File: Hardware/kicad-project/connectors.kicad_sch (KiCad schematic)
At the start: 25 parts, among them CN10 Conn_02x17_Odd_Even, CN7 Conn_02x10_Odd_Even, CN8 Conn_02x08_Odd_Even, CN9 Conn_02x15_Odd_Even, J1 Brake connector, J2 Conn_01x08, J3 PWM module connector, J5 UART Connector, J6 Stepper supply, Q1 Q_NMOS_DGS

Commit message: hw: update layout corrections
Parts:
- Q1: symbol Device:Q_NMOS_DGS -> Device:Q_NMOS_GDS
- TP1: renamed from TP_24V; value TestPoint -> 24V
- TP2: renamed from TP_TORQUE; value TestPoint -> TORQUE
- TP3: renamed from TP_12V; value TestPoint -> 12V
- TP4: renamed from TP_5V; value TestPoint -> 5V
- TP5: renamed from TP_BRAKE; value TestPoint -> BRAKE
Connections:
- net UART1_RX: now also CN10.16 (Pin_16); no longer CN7.3 (Pin_3)
- net at R4.1: now also Q1.2 (D); no longer Q1.1 (D)
- net at R1.2, R3.2: now also Q1.1 (G); no longer Q1.2 (G)
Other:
- note added: "UART & STEPPER CONNECTORS"
- note removed: "UART & STEPPER CONENCTORS"
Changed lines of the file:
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@@
   (no_connect (at 98.425 39.37))
   (no_connect (at 85.09 114.3))
-  (no_connect (at 97.79 91.44))
+  (no_connect (at 85.725 41.91))
   (no_connect (at 36.83 46.99))
   (no_connect (at 85.09 81.28))
@@
     (stroke (width 0) (type default) (color 0 0 0 0))
   )
-  (wire (pts (xy 74.93 41.91) (xy 85.725 41.91))
+  (wire (pts (xy 108.585 91.44) (xy 97.79 91.44))
     (stroke (width 0) (type default) (color 0 0 0 0))
   )
@@
     (effects (font (size 1.27 1.27) italic) (justify left bottom))
   )
-  (text "UART & STEPPER CONENCTORS" (at 126.365 70.485 0)
+  (text "UART & STEPPER CONNECTORS" (at 126.365 70.485 0)
     (effects (font (size 2 2) bold) (justify left bottom))
   )
@@
     (effects (font (size 1.27 1.27)) (justify left bottom))
   )
-  (label "UART1_RX" (at 74.93 41.91 0)
-    (effects (font (size 1.27 1.27)) (justify left bottom))
+  (label "UART1_RX" (at 108.585 91.44 180)
+    (effects (font (size 1.27 1.27)) (justify right bottom))
   )
   (label "LED1" (at 92.075 146.685 270)
@@
   (symbol (lib_id "Connector:TestPoint") (at 47.625 152.4 180) (unit 1)
     (in_bom yes) (on_board yes) (fields_autoplaced)
-    (property "Reference" "TP_12V" (id 0) (at 49.53 154.4319 0)
-      (effects (font (size 1.27 1.27)) (justify right))
-    )
-    (property "Value" "TestPoint" (id 1) (at 49.53 156.9719 0)
+    (property "Reference" "TP3" (id 0) (at 49.53 154.4319 0)
+      (effects (font (size 1.27 1.27)) (justify right))
+    )
+    (property "Value" "12V" (id 1) (at 49.53 156.9719 0)
       (effects (font (size 1.27 1.27)) (justify right))
     )
@@
   (symbol (lib_id "Connector:TestPoint") (at 62.865 152.4 180) (unit 1)
     (in_bom yes) (on_board yes) (fields_autoplaced)
-    (property "Reference" "TP_5V" (id 0) (at 64.77 154.4319 0)
-      (effects (font (size 1.27 1.27)) (justify right))
-    )
-    (property "Value" "TestPoint" (id 1) (at 64.77 156.9719 0)
+    (property "Reference" "TP4" (id 0) (at 64.77 154.4319 0)
+      (effects (font (size 1.27 1.27)) (justify right))
+    )
+    (property "Value" "5V" (id 1) (at 64.77 156.9719 0)
       (effects (font (size 1.27 1.27)) (justify right))
     )
@@
     (pin "1")
   )
-  (symbol (lib_id "Device:Q_NMOS_DGS") (at 211.455 140.335 0) (unit 1)
+  (symbol (lib_id "Device:Q_NMOS_GDS") (at 211.455 140.335 0) (unit 1)
     (in_bom yes) (on_board yes) (fields_autoplaced)
     (property "Reference" "Q1" (id 0) (at 217.17 139.0649 0)
@@
       (effects (font (size 1.27 1.27)) hide)
     )
-    (property "Datasheet" "https://www.mouser.it/datasheet/2/196/Infineon-IPD60N10S4L_12-DS-v01_00-en-1731716.pdf" (id 3) (at 211.455 140.335 0)
+    (property "Datasheet" "~" (id 3) (at 211.455 140.335 0)
       (effects (font (size 1.27 1.27)) hide)
     )
@@
   (symbol (lib_id "Connector:TestPoint") (at 33.655 152.4 180) (unit 1)
     (in_bom yes) (on_board yes) (fields_autoplaced)
-    (property "Reference" "TP_24V" (id 0) (at 35.56 154.4319 0)
-      (effects (font (size 1.27 1.27)) (justify right))
-    )
-    (property "Value" "TestPoint" (id 1) (at 35.56 156.9719 0)
+    (property "Reference" "TP1" (id 0) (at 35.56 154.4319 0)
+      (effects (font (size 1.27 1.27)) (justify right))
+    )
+    (property "Value" "24V" (id 1) (at 35.56 156.9719 0)
       (effects (font (size 1.27 1.27)) (justify right))
     )
@@
   (symbol (lib_id "Connector:TestPoint") (at 40.64 170.18 180) (unit 1)
     (in_bom yes) (on_board yes) (fields_autoplaced)
-    (property "Reference" "TP_TORQUE" (id 0) (at 43.18 172.2119 0)
-      (effects (font (size 1.27 1.27)) (justify right))
-    )
-    (property "Value" "TestPoint" (id 1) (at 43.18 174.7519 0)
+    (property "Reference" "TP2" (id 0) (at 43.18 172.2119 0)
+      (effects (font (size 1.27 1.27)) (justify right))
+    )
+    (property "Value" "TORQUE" (id 1) (at 43.18 174.7519 0)
       (effects (font (size 1.27 1.27)) (justify right))
     )
@@
   (symbol (lib_id "Connector:TestPoint") (at 63.5 170.815 180) (unit 1)
     (in_bom yes) (on_board yes) (fields_autoplaced)
-    (property "Reference" "TP_BRAKE" (id 0) (at 65.405 172.8469 0)
-      (effects (font (size 1.27 1.27)) (justify right))
-    )
-    (property "Value" "TestPoint" (id 1) (at 65.405 175.3869 0)
-      (effects (font (size 1.27 1.27)) (justify right))
-    )
+    (property "Reference" "TP5" (id 0) (at 66.04 172.8469 0)
+      (effects (font (size 1.27 1.27)) (justify right))
+    )
+    (property "Value" "BRAKE" (id 1) (at 66.04 175.3869 0)
+      (effects (font (size 1.27 1.27)) (justify right))
+    )

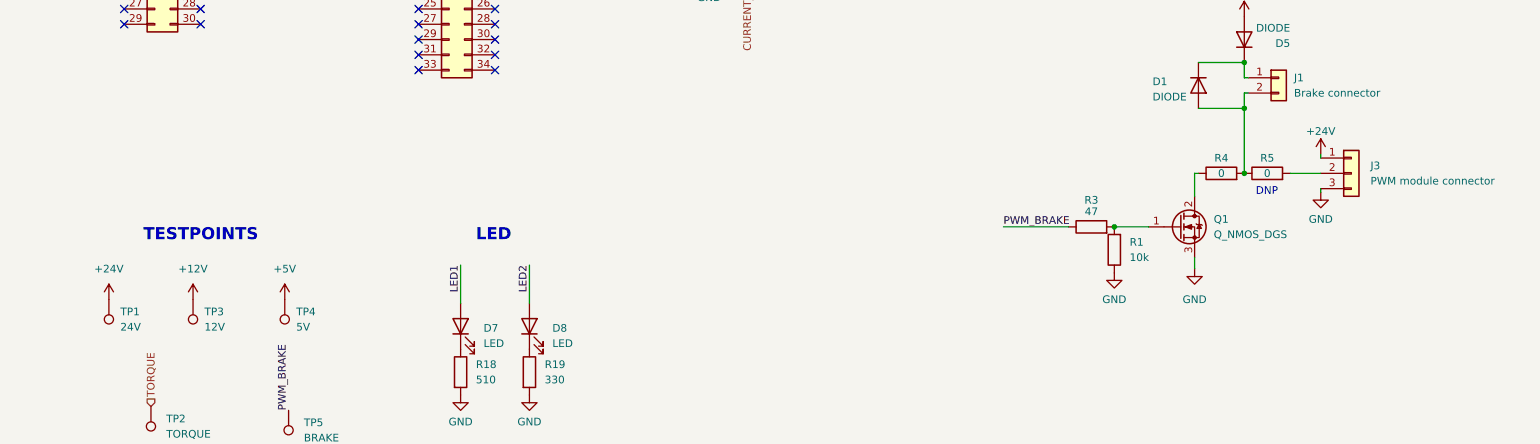
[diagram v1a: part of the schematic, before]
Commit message: hw: update layout with right screw terminal
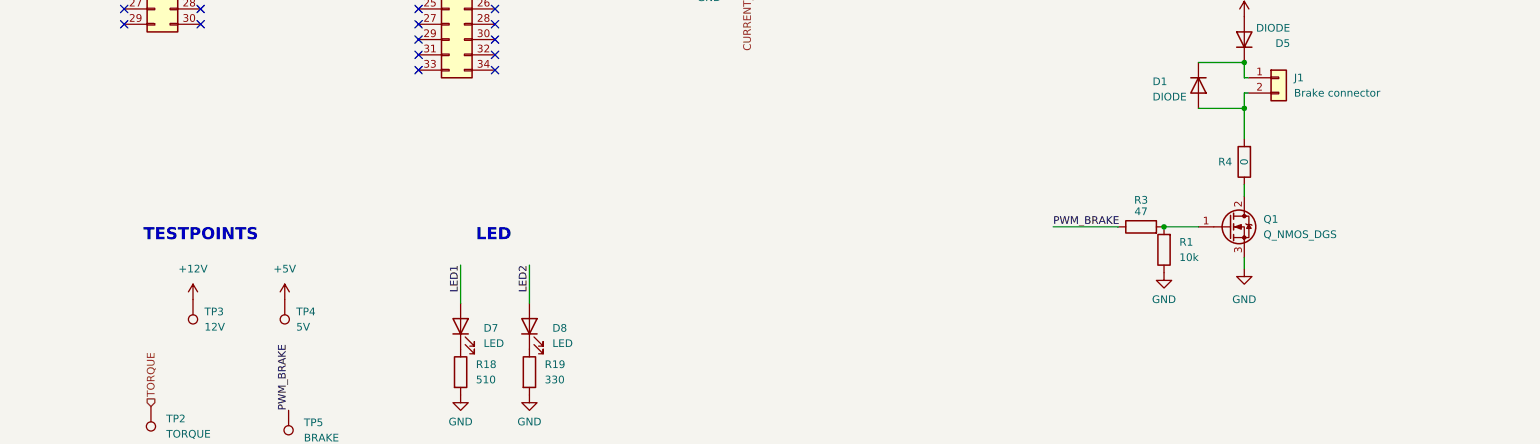
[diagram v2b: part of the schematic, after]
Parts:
- removed J3: PWM module connector, Connector_PinHeader_2.54mm:PinHeader_1x03_P2.54mm_Vertical, symbol Connector_Generic:Conn_01x03
- removed R5: 0, Resistor_SMD:R_0603_1608Metric, symbol Device:R
- removed TP1: 24V, TestPoint:TestPoint_Pad_D2.0mm, symbol Connector:TestPoint
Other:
- note removed: "DNP"
- moved on the sheet: Q1, R1, R3, R4

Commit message: hw: final pdf schematic upload
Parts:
- removed TP4: 5V, TestPoint:TestPoint_Pad_D2.0mm, symbol Connector:TestPoint
- added Q2: Q_NMOS_DGS, Package_TO_SOT_SMD:TO-252-2, symbol Device:Q_NMOS_GDS
- added R28: 10k, Resistor_SMD:R_0603_1608Metric, symbol Device:R
- added R5: 47, Resistor_SMD:R_0603_1608Metric, symbol Device:R
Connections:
- net +24V: no longer J6.1 (Pin_1)
- net CURRENT_ADC: now also CN7.10 (Pin_10); no longer CN9.1 (Pin_1)
- net GND: now also Q2.3 (S), R28.1; no longer J6.2 (Pin_2)
- net LED1: now also CN9.26 (Pin_26); no longer CN9.16 (Pin_16)
- net LED2: now also CN9.28 (Pin_28); no longer CN9.18 (Pin_18)
- net PWM_BRAKE: now also CN8.2 (Pin_2); no longer CN7.12 (Pin_12)
- net TORQUE_ADC: now also CN9.1 (Pin_1); no longer CN9.5 (Pin_5)
- net VOLTAGE_STEPPER_ADC: now also CN9.5 (Pin_5); no longer CN7.10 (Pin_10)
- net 24V_BRAKE: now reaches D1.2 (K), D5.2 (K), J1.1 (Pin_1)
- net DISABLE_STEPPER_SUPPLY: now reaches CN8.4 (Pin_4)
- net DISABLE_STEPPER_SUPPLY: now also R5.1
- new net: J6.2 (Pin_2), Q2.2 (D)
- new net: Q2.1 (G), R28.2, R5.2
- new net STEPPER+: J6.1 (Pin_1)
- no-connect marks 95 -> 94
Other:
- moved on the sheet: D1, D5, D7, D8, J1, J2, J5, J6, Q1, R1, R18, R19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

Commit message: hw: layout v0.1.1
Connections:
- net DISABLE_STEPPER_SUPPLY renamed ENABLE_STEPPER_SUPPLY
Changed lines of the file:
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@@
     (effects (font (size 1.27 1.27)) (justify left bottom))
   )
-  (label "DISABLE_STEPPER_SUPPLY" (at 123.825 67.31 0)
+  (label "ENABLE_STEPPER_SUPPLY" (at 123.825 67.31 0)
     (effects (font (size 1.27 1.27)) (justify left bottom))
   )
@@
     (effects (font (size 1.27 1.27)) (justify left bottom))
   )
-  (label "DISABLE_STEPPER_SUPPLY" (at 74.93 41.91 180)
+  (label "ENABLE_STEPPER_SUPPLY" (at 74.93 41.91 180)
     (effects (font (size 1.27 1.27)) (justify right bottom))
   )
